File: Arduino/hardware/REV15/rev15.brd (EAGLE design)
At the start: 50 x 50 mm, 20 parts, among them IC2 ATMEGA168-AU, Q1 32768Hz

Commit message: up to rev18 cleaned up
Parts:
- moved U$2 26.7 mm to (-7.75, 27.1)
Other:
- board text removed: "Seal off solderpads with hotmelt glue or silicone glue"
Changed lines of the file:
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@@
 <plain>
 <text x="-5.318971875" y="13.33876875" size="1" layer="25" font="vector" rot="R180">20151208</text>
-<text x="24.149196875" y="-4.224378125" size="1" layer="22" font="vector" rot="MR0">License: http://goo.gl/3d71UJ</text>
-<text x="12.333878125" y="-0.70546875" size="1" layer="25" font="vector" rot="R180">OpenTRV.org.uk</text>
-<text x="-6.35" y="45.72" size="1" layer="26" rot="MR270">Seal off solderpads with
- hotmelt glue or silicone
- glue</text>
+<text x="36.849196875" y="0.855621875" size="1" layer="22" font="vector" rot="MR0">License: http://goo.gl/3d71UJ</text>
+<text x="31.383878125" y="1.83453125" size="1" layer="25" font="vector" rot="R180">OpenTRV.org.uk</text>
 <wire x1="0" y1="0" x2="0" y2="50" width="0.4064" layer="20"/>
 <wire x1="0" y1="50" x2="50" y2="50" width="0.4064" layer="20"/>
 <wire x1="50" y1="50" x2="50" y2="0" width="0.4064" layer="20"/>
 <wire x1="50" y1="0" x2="0" y2="0" width="0.4064" layer="20"/>
-<text x="2.085" y="41.655" size="1" layer="25">DQ</text>
+<text x="2.085" y="41.655" size="1" layer="25" font="vector">DQ</text>
 </plain>
 <attributes>
@@
 <attribute name="NAME" x="17.440165625" y="5.0265" size="1" layer="25" font="vector" rot="R90"/>
 </element>
-<element name="U$2" library="logo" package="TONNE" value="" x="-9.025" y="53.75711875"/>
+<element name="U$2" library="logo" package="TONNE" value="" x="-7.755" y="27.08711875"/>
 <element name="R2" library="resistor" package="R0603" value="4.7K" x="30.006046875" y="29.3970875" smashed="yes" rot="R270">
 <attribute name="NAME" x="30.47489375" y="31.03400625" size="1" layer="25" font="vector" rot="R90"/>
@@
 </element>
 <element name="IC2" library="Arduino-AVR" package="TQFP32-08" value="ATMEGA168-AU" x="30.48" y="20.32" smashed="yes">
-<attribute name="NAME" x="29.6164" y="19.685" size="1" layer="25"/>
+<attribute name="NAME" x="29.6164" y="19.685" size="1" layer="25" font="vector"/>
 </element>
 <element name="R6" library="resistor" package="R0603" value="100K" x="33.02" y="4.445" smashed="yes" rot="R180">
-<attribute name="NAME" x="33.274" y="2.921" size="1" layer="25" rot="R180"/>
+<attribute name="NAME" x="33.274" y="2.921" size="1" layer="25" font="vector" rot="R180"/>
 </element>
 <element name="PHT" library="opto-trans-siemens" package="BPX65" value="BPX65" x="40.89" y="5.715" smashed="yes" rot="R45">
@@
 <attribute name="OC_NEWARK" value="06WX2764" x="45.380125" y="1.224871875" size="1.778" layer="27" rot="R45" display="off"/>
 <attribute name="MPN" value="BPX65." x="45.380125" y="1.224871875" size="1.778" layer="27" rot="R45" display="off"/>
-<attribute name="NAME" x="37.420059375" y="4.1500625" size="1" layer="25" rot="R90"/>
+<attribute name="NAME" x="37.420059375" y="4.1500625" size="1" layer="25" font="vector" rot="R90"/>
 </element>
 <element name="R9" library="resistor" package="R0603" value="4.7K" x="17.52" y="39.37" smashed="yes" rot="R90">
-<attribute name="NAME" x="17.024" y="37.465" size="1" layer="25" rot="R270"/>
+<attribute name="NAME" x="17.024" y="37.465" size="1" layer="25" font="vector" rot="R270"/>
 </element>
 <element name="R4" library="resistor" package="R0603" value="4K7" x="22.86" y="39.37" smashed="yes" rot="R90">
-<attribute name="NAME" x="23.241" y="35.941" size="1" layer="25" rot="R90"/>
+<attribute name="NAME" x="23.241" y="35.941" size="1" layer="25" font="vector" rot="R90"/>
 </element>
 <element name="R8" library="resistor" package="R0603" value="4K7" x="27.305" y="39.37" smashed="yes" rot="R180">
-<attribute name="NAME" x="30.734" y="39.751" size="1" layer="25" rot="R180"/>
+<attribute name="NAME" x="30.734" y="39.751" size="1" layer="25" font="vector" rot="R180"/>
 </element>
 <element name="DQ" library="wirepad" package="2,15/1,0" value="" x="3.81" y="44.45" smashed="yes">
@@
 </element>
 <element name="R1" library="resistor" package="R0603" value="4.7K" x="15.24" y="39.37" smashed="yes" rot="R270">
-<attribute name="NAME" x="14.605" y="37.465" size="1" layer="25" rot="R270"/>
+<attribute name="NAME" x="14.605" y="37.465" size="1" layer="25" font="vector" rot="R270"/>
 </element>
 <element name="R3" library="resistor" package="R0603" value="4.7K" x="20.32" y="39.37" smashed="yes" rot="R270">
-<attribute name="NAME" x="19.685" y="37.465" size="1" layer="25" rot="R270"/>
+<attribute name="NAME" x="19.685" y="37.465" size="1" layer="25" font="vector" rot="R270"/>
 </element>
 <element name="C5" library="resistor" package="C0603" value="100nF" x="12.7" y="39.37" smashed="yes" rot="R90">
-<attribute name="NAME" x="12.065" y="37.465" size="1" layer="25" rot="R270"/>
+<attribute name="NAME" x="12.065" y="37.465" size="1" layer="25" font="vector" rot="R270"/>
 </element>
 </elements>
@@
 <via x="47.832378125" y="2.0994875" extent="1-16" drill="3.2"/>
 <via x="2.112378125" y="2.0994875" extent="1-16" drill="3.2"/>
+<via x="16.51" y="21.59" extent="1-16" drill="0.5"/>
+<via x="17.78" y="21.59" extent="1-16" drill="0.5"/>
+<via x="19.05" y="21.59" extent="1-16" drill="0.5"/>
+<via x="20.32" y="21.59" extent="1-16" drill="0.5"/>
+<via x="21.59" y="21.59" extent="1-16" drill="0.5"/>
+<via x="22.225" y="20.32" extent="1-16" drill="0.5"/>
+<via x="22.225" y="19.05" extent="1-16" drill="0.5"/>
+<via x="15.24" y="21.59" extent="1-16" drill="0.5"/>
+<via x="13.97" y="21.59" extent="1-16" drill="0.5"/>
+<via x="12.7" y="21.59" extent="1-16" drill="0.5"/>
+<via x="12.7" y="20.32" extent="1-16" drill="0.5"/>
+<via x="12.7" y="19.05" extent="1-16" drill="0.5"/>
+<via x="12.7" y="17.78" extent="1-16" drill="0.5"/>
+<via x="12.7" y="16.51" extent="1-16" drill="0.5"/>
+<via x="12.7" y="15.24" extent="1-16" drill="0.5"/>
+<via x="13.97" y="14.605" extent="1-16" drill="0.5"/>
+<via x="15.24" y="14.605" extent="1-16" drill="0.5"/>
+<via x="16.51" y="14.605" extent="1-16" drill="0.5"/>
+<via x="17.78" y="14.605" extent="1-16" drill="0.5"/>
+<via x="19.05" y="14.605" extent="1-16" drill="0.5"/>
+<via x="20.32" y="14.605" extent="1-16" drill="0.5"/>
+<via x="21.59" y="14.605" extent="1-16" drill="0.5"/>
+<via x="22.225" y="15.875" extent="1-16" drill="0.5"/>
 </signal>
 <signal name="SPI_SCK">
@@
 <via x="19.1008" y="38.608" extent="1-16" drill="0.5"/>
 </signal>
-<signal name="N$28">
-<via x="22.225" y="15.875" extent="1-16" drill="0.5"/>
-</signal>
-<signal name="N$35">
-<via x="12.7" y="16.51" extent="1-16" drill="0.5"/>
-</signal>
-<signal name="N$36">
-<via x="12.7" y="15.24" extent="1-16" drill="0.5"/>
-</signal>
-<signal name="N$37">
-<via x="13.97" y="14.605" extent="1-16" drill="0.5"/>
-</signal>
-<signal name="N$38">
-<via x="15.24" y="14.605" extent="1-16" drill="0.5"/>
-</signal>
-<signal name="N$39">
-<via x="16.51" y="14.605" extent="1-16" drill="0.5"/>
-</signal>
-<signal name="N$40">
-<via x="17.78" y="14.605" extent="1-16" drill="0.5"/>
-</signal>
-<signal name="N$41">
-<via x="19.05" y="14.605" extent="1-16" drill="0.5"/>
-</signal>
-<signal name="N$42">
-<via x="12.7" y="17.78" extent="1-16" drill="0.5"/>
-</signal>
-<signal name="N$43">
-<via x="12.7" y="19.05" extent="1-16" drill="0.5"/>
-</signal>
-<signal name="N$44">
-<via x="12.7" y="20.32" extent="1-16" drill="0.5"/>
-</signal>
-<signal name="N$45">
-<via x="12.7" y="21.59" extent="1-16" drill="0.5"/>
-</signal>
-<signal name="N$46">
-<via x="13.97" y="21.59" extent="1-16" drill="0.5"/>
-</signal>
-<signal name="N$47">
-<via x="15.24" y="21.59" extent="1-16" drill="0.5"/>
-</signal>
-<signal name="N$48">
-<via x="16.51" y="21.59" extent="1-16" drill="0.5"/>
-</signal>
-<signal name="N$49">
-<via x="17.78" y="21.59" extent="1-16" drill="0.5"/>
-</signal>
-<signal name="N$50">
-<via x="19.05" y="21.59" extent="1-16" drill="0.5"/>
-</signal>
-<signal name="N$51">
-<via x="20.32" y="21.59" extent="1-16" drill="0.5"/>
-</signal>
-<signal name="N$52">
-<via x="21.59" y="14.605" extent="1-16" drill="0.5"/>
-</signal>
-<signal name="N$53">
-<via x="22.225" y="20.32" extent="1-16" drill="0.5"/>
-</signal>
-<signal name="N$54">
-<via x="22.23" y="19.08" extent="1-16" drill="0.5"/>
-</signal>
-<signal name="N$33">
-<via x="20.32" y="14.605" extent="1-16" drill="0.5"/>
-</signal>
-<signal name="N$34">
-<via x="21.59" y="21.59" extent="1-16" drill="0.5"/>
-</signal>
 <signal name="N$26">
 <contactref element="I2C_EXT" pad="20"/>
@@
 </board>
 </drawing>
-<compatibility>
-<note version="6.3" minversion="6.2.2" severity="warning">
-Since Version 6.2.2 text objects can contain more than one line,
-which will not be processed correctly with this version.
-</note>
-</compatibility>
 </eagle>

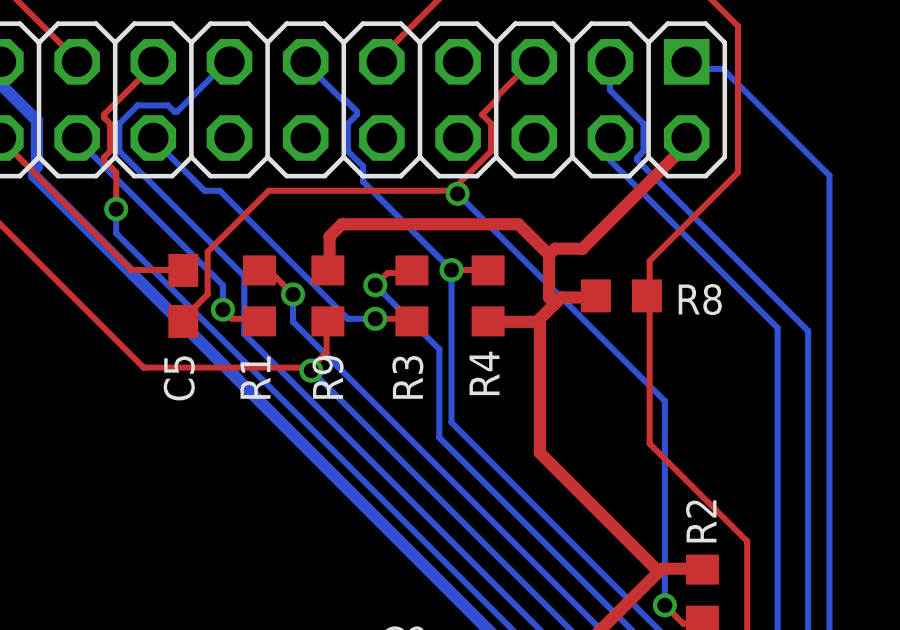
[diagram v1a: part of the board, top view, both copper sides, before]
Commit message: up to rev18 DRC check and ground plane
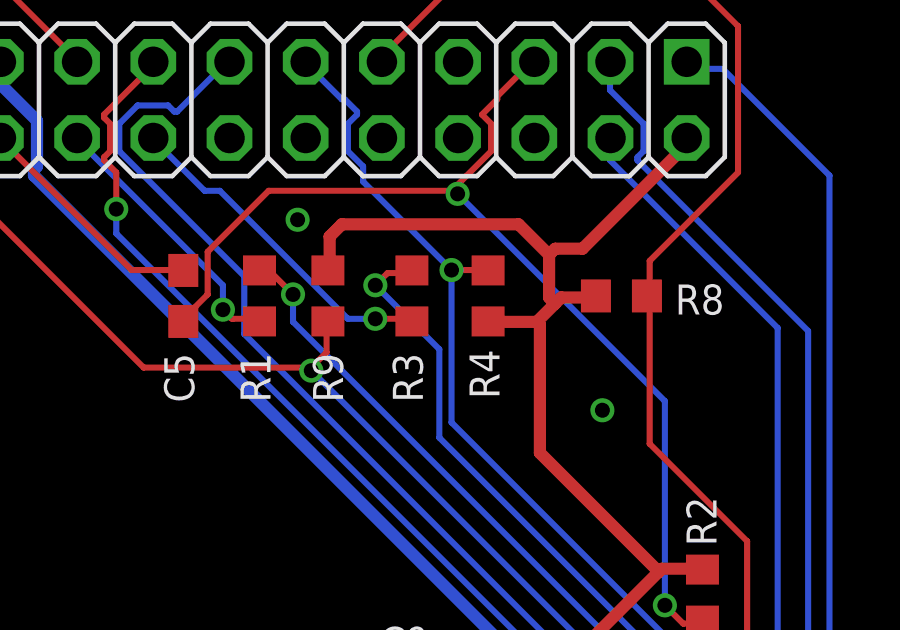
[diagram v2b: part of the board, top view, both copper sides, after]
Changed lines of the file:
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@@
 <via x="21.59" y="14.605" extent="1-16" drill="0.5"/>
 <via x="22.225" y="15.875" extent="1-16" drill="0.5"/>
+<via x="26.67" y="35.56" extent="1-16" drill="0.5"/>
+<via x="16.51" y="41.91" extent="1-16" drill="0.5"/>
 </signal>
 <signal name="SPI_SCK">

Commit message: REV15-18 cleaned up, need sanity check
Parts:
- moved U$2 49.8 mm to (41.8, 32.2)
- moved U$1 18.3 mm to (4.51, 26.2)
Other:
- board text added: "20160229"
- board text removed: "20151208"
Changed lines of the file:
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@@
 <board>
 <plain>
-<text x="-5.318971875" y="13.33876875" size="1" layer="25" font="vector" rot="R180">20151208</text>
+<text x="47.62123125" y="12.461028125" size="1" layer="25" font="vector" rot="R270">20160229</text>
 <text x="36.849196875" y="0.855621875" size="1" layer="22" font="vector" rot="MR0">License: http://goo.gl/3d71UJ</text>
 <text x="31.383878125" y="1.83453125" size="1" layer="25" font="vector" rot="R180">OpenTRV.org.uk</text>
@@
 <attribute name="NAME" x="17.440165625" y="5.0265" size="1" layer="25" font="vector" rot="R90"/>
 </element>
-<element name="U$2" library="logo" package="TONNE" value="" x="-7.755" y="27.08711875"/>
+<element name="U$2" library="logo" package="TONNE" value="" x="41.775" y="32.16711875"/>
 <element name="R2" library="resistor" package="R0603" value="4.7K" x="30.006046875" y="29.3970875" smashed="yes" rot="R270">
 <attribute name="NAME" x="30.47489375" y="31.03400625" size="1" layer="25" font="vector" rot="R90"/>
@@
 <attribute name="NAME" x="41.212525" y="15.8739" size="1" layer="25" font="vector" rot="R180"/>
 </element>
-<element name="U$1" library="ohw-logo" package="OSHW_10X200_NOTEXT" value="" x="-10.725834375" y="16.02610625"/>
+<element name="U$1" library="ohw-logo" package="OSHW_10X200_NOTEXT" value="" x="4.514165625" y="26.18610625"/>
 <element name="C12" library="resistor" package="C0603" value="100nF" x="40.08" y="21.19" smashed="yes">
 <attribute name="NAME" x="41.160225" y="19.938" size="1" layer="25" font="vector" rot="R180"/>
